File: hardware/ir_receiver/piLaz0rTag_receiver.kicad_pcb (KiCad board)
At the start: 2 copper layers, 5 parts

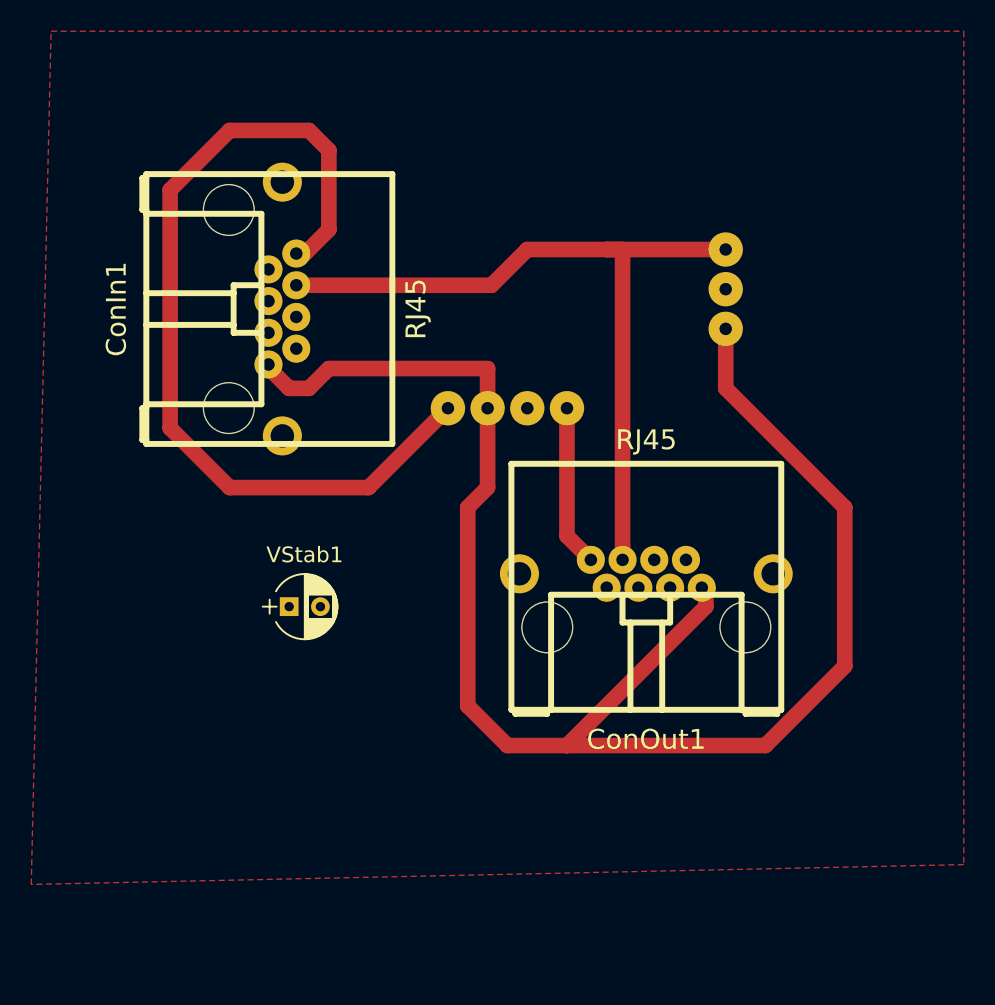
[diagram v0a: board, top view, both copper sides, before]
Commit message: Add Dome as drawing
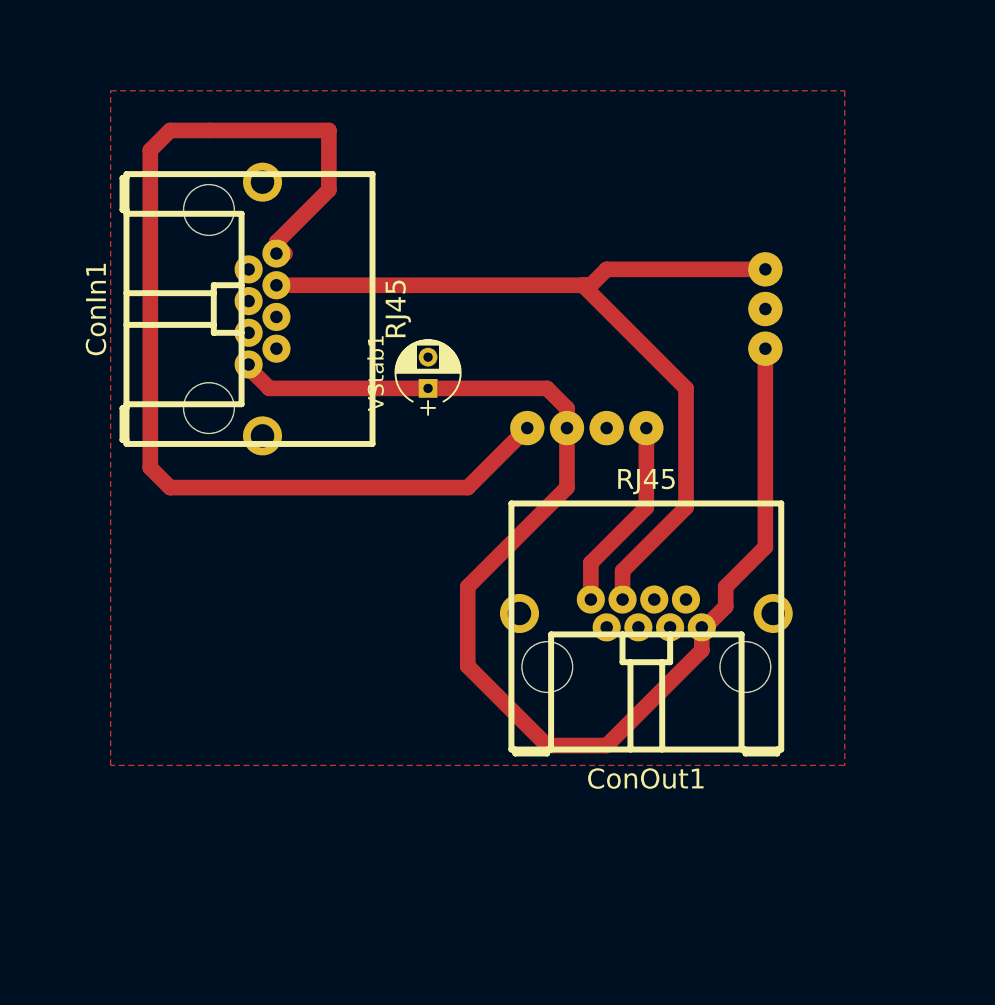
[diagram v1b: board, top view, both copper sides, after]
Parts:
- moved VStab1 16.6 mm to (97.8, 102.9), turned to 90 degrees
- moved LED1 5.24 mm to (111.8, 105.4)
- moved IR_REC1 2.84 mm to (119.4, 95.2)
- moved ConOut1 2.54 mm to (111.8, 118.1)
- moved ConIn1 1.27 mm to (86.4, 97.8)
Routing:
- net +5V: track 103.8 -> 81.9 mm
- net /LedIn: track 57.1 -> 68.7 mm
- net /IrData: track 49.7 -> 57.1 mm
- net /LedOut: track 10.7 -> 12.8 mm

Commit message: First thing to test
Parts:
- added REF**: MountingHole_2.2mm_M2_DIN965, Mounting_Holes:MountingHole_2.2mm_M2_DIN965, F.Cu at (104.1, 99.7)
- added REF**: MountingHole_2.2mm_M2, Mounting_Holes:MountingHole_2.2mm_M2, F.Cu at (115.6, 98.4)
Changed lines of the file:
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@@
 (kicad_pcb (version 4) (host pcbnew 4.0.7-e2-6376~61~ubuntu18.04.1)
   (general
-    (links 18)
-    (no_connects 4)
-    (area 72.39 80.01 132.080001 134.620001)
+    (links 20)
+    (no_connects 5)
+    (area 74.8618 83.82 125.427143 142.400001)
     (thickness 1.6)
     (drawings 8)
     (tracks 45)
     (zones 0)
-    (modules 5)
+    (modules 7)
     (nets 12)
   )
@@
     (mod_text_width 0.15)
     (pad_size 2.2 2.2)
-    (pad_drill 0.8)
+    (pad_drill 0.9)
     (pad_to_mask_clearance 0.2)
     (aux_axis_origin 77.47 127)
@@
     )
   )
+  (module Mounting_Holes:MountingHole_2.2mm_M2_DIN965 (layer F.Cu)
+    (at 104.14 99.695)
+    (descr "Mounting Hole 2.2mm, no annular, M2, DIN965")
+    (tags "mounting hole 2.2mm no annular m2 din965")
+    (fp_text reference REF** (at 0 -2.9) (layer F.SilkS)
+      (effects (font (size 1 1) (thickness 0.15)))
+    )
+    (fp_text value MountingHole_2.2mm_M2_DIN965 (at 0 2.9) (layer F.Fab)
+      (effects (font (size 1 1) (thickness 0.15)))
+    )
+    (fp_circle (center 0 0) (end 1.9 0) (layer Cmts.User) (width 0.15))
+    (fp_circle (center 0 0) (end 2.15 0) (layer F.CrtYd) (width 0.05))
+    (pad 1 thru_hole circle (at 0 0) (size 2.2 2.2) (drill 0.9) (layers *.Cu *.Mask)
+      (net 2 GND))
+  )
+  (module Mounting_Holes:MountingHole_2.2mm_M2 (layer F.Cu)
+    (at 115.57 98.425)
+    (descr "Mounting Hole 2.2mm, no annular, M2")
+    (tags "mounting hole 2.2mm no annular m2")
+    (fp_text reference REF** (at 0 -3.2) (layer F.SilkS)
+      (effects (font (size 1 1) (thickness 0.15)))
+    )
+    (fp_text value MountingHole_2.2mm_M2 (at 0 3.2) (layer F.Fab)
+      (effects (font (size 1 1) (thickness 0.15)))
+    )
+    (fp_circle (center 0 0) (end 2.2 0) (layer Cmts.User) (width 0.15))
+    (fp_circle (center 0 0) (end 2.45 0) (layer F.CrtYd) (width 0.05))
+    (pad 1 thru_hole circle (at 0 0) (size 2.2 2.2) (drill 0.9) (layers *.Cu *.Mask)
+      (net 2 GND))
+  )
   (dimension 21.59 (width 0.3) (layer Dwgs.User)
     (gr_text "21,590 mm" (at 89.535 135.97) (layer Dwgs.User)
@@
   (gr_line (start 101.6 97.79) (end 101.6 87.63) (angle 90) (layer Dwgs.User) (width 0.2))
   (gr_circle (center 111.76 97.73) (end 111.76 87.73) (layer Dwgs.User) (width 0.2))
-  (segment (start 115.31092 118.16588) (end 115.51412 118.16588) (width 1) (layer F.Cu) (net 1) (status C00000))
-  (segment (start 115.51412 118.16588) (end 116.84 116.84) (width 1) (layer F.Cu) (net 1) (status 400000))
-  (segment (start 119.38 113.03) (end 119.38 100.33) (width 1) (layer F.Cu) (net 1) (status 800000))
+  (segment (start 115.31092 118.16588) (end 115.51412 118.16588) (width 1) (layer F.Cu) (net 1))
+  (segment (start 115.51412 118.16588) (end 116.84 116.84) (width 1) (layer F.Cu) (net 1))
+  (segment (start 119.38 113.03) (end 119.38 100.33) (width 1) (layer F.Cu) (net 1))
   (segment (start 116.84 115.57) (end 119.38 113.03) (width 1) (layer F.Cu) (net 1))
   (segment (start 116.84 116.84) (end 116.84 115.57) (width 1) (layer F.Cu) (net 1))

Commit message: First thing to test
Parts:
- ConIn1, ConOut1, REF** (x2), VStab1: moved to B.Cu
- IR_REC1, LED1: moved to F.Cu
- moved IR_REC1 33.7 mm to (119.4, 128.9), turned to 90 degrees
- moved ConIn1 28.6 mm to (86.4, 126.4), turned to 90 degrees
- moved REF** 27.3 mm to (115.6, 125.7)
- moved REF** 24.8 mm to (104.1, 124.5)
- moved VStab1 18.4 mm to (97.8, 121.3), turned to 270 degrees
- moved LED1 13.3 mm to (111.8, 118.7), turned to 270 degrees
- moved ConOut1 12.1 mm to (111.8, 106.0)
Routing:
- added copper zone on B.Cu, net GND
- removed copper zone on F.Cu, net GND

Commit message: First thing to test
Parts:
- removed REF**: MountingHole_2.2mm_M2_DIN965, Mounting_Holes:MountingHole_2.2mm_M2_DIN965
- removed REF**: MountingHole_2.2mm_M2, Mounting_Holes:MountingHole_2.2mm_M2
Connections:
- ConIn1 pad 13: Net-(ConIn1-Pad13) -> GND
- ConIn1 pad 2: Net-(ConIn1-Pad2) -> GND
- ConIn1 pad 3: Net-(ConIn1-Pad3) -> GND
- ConOut1 pad 13: Net-(ConOut1-Pad13) -> GND
- ConOut1 pad 2: Net-(ConOut1-Pad2) -> GND
- ConOut1 pad 3: Net-(ConOut1-Pad3) -> GND
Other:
- net class Default: via_dia 0.6 -> 1; via_drill 0.4 -> 0.9
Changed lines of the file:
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@@
 (kicad_pcb (version 4) (host pcbnew 4.0.7-e2-6376~61~ubuntu18.04.1)
   (general
-    (links 20)
-    (no_connects 4)
-    (area 74.8618 83.82 125.427143 142.400001)
+    (links 24)
+    (no_connects 1)
+    (area 74.8618 94.5468 124.690001 140.335001)
     (thickness 1.6)
     (drawings 6)
-    (tracks 45)
+    (tracks 44)
     (zones 0)
-    (modules 7)
-    (nets 12)
+    (modules 5)
+    (nets 6)
   )
   (page A4)
@@
     (segment_width 0.2)
     (edge_width 0.15)
-    (via_size 0.6)
-    (via_drill 0.4)
+    (via_size 1)
+    (via_drill 0.9)
     (via_min_size 0.4)
     (via_min_drill 0.3)
@@
     (mod_text_size 1 1)
     (mod_text_width 0.15)
-    (pad_size 2.2 2.2)
-    (pad_drill 0.9)
+    (pad_size 0.8 0.8)
+    (pad_drill 0.8)
     (pad_to_mask_clearance 0.2)
     (aux_axis_origin 77.47 127)
@@
   (net 4 /LedIn)
   (net 5 /LedOut)
-  (net 6 "Net-(ConIn1-Pad2)")
-  (net 7 "Net-(ConIn1-Pad13)")
-  (net 8 "Net-(ConOut1-Pad2)")
-  (net 9 "Net-(ConOut1-Pad13)")
-  (net 10 "Net-(ConIn1-Pad3)")
-  (net 11 "Net-(ConOut1-Pad3)")
   (net_class Default "This is the default net class."
     (clearance 0.5)
     (trace_width 1)
-    (via_dia 0.6)
-    (via_drill 0.4)
+    (via_dia 1)
+    (via_drill 0.9)
     (uvia_dia 0.3)
     (uvia_drill 0.1)
@@
     (add_net /LedOut)
     (add_net GND)
-    (add_net "Net-(ConIn1-Pad13)")
-    (add_net "Net-(ConIn1-Pad2)")
-    (add_net "Net-(ConIn1-Pad3)")
-    (add_net "Net-(ConOut1-Pad13)")
-    (add_net "Net-(ConOut1-Pad2)")
-    (add_net "Net-(ConOut1-Pad3)")
   )
   (module kicad:rj45-seppel-small (layer B.Cu)
@@
     (fp_line (start 8.636 7.874) (end 8.636 -7.874) (layer B.SilkS) (width 0.381))
     (fp_line (start 8.636 -7.874) (end -8.636 -7.874) (layer B.SilkS) (width 0.381))
-    (pad 3 thru_hole circle (at 1.52146 -0.05588) (size 1.8 1.8) (drill 0.8001) (layers *.Cu *.Mask)
-      (net 11 "Net-(ConOut1-Pad3)"))
-    (pad 1 thru_hole circle (at 3.55092 -0.05588) (size 1.8 1.8) (drill 0.8001) (layers *.Cu *.Mask)
+    (pad 3 thru_hole circle (at 1.52146 -0.05588) (size 0.8 0.8) (drill 0.8) (layers *.Cu *.Mask)
+      (net 2 GND))
+    (pad 1 thru_hole circle (at 3.55092 -0.05588) (size 2.2 2.2) (drill 0.8) (layers *.Cu *.Mask)
       (net 1 +5V))
-    (pad 2 thru_hole circle (at 2.53746 1.72466) (size 1.8 1.8) (drill 0.8001) (layers *.Cu *.Mask)
-      (net 8 "Net-(ConOut1-Pad2)"))
-    (pad 4 thru_hole circle (at 0.508 1.72466) (size 1.8 1.8) (drill 0.8001) (layers *.Cu *.Mask)
-      (net 2 GND))
-    (pad 5 thru_hole circle (at -0.508 -0.05588) (size 1.8 1.8) (drill 0.8001) (layers *.Cu *.Mask)
+    (pad 2 thru_hole circle (at 2.53746 1.72466) (size 0.8 0.8) (drill 0.8) (layers *.Cu *.Mask)
+      (net 2 GND))
+    (pad 4 thru_hole circle (at 0.508 1.72466) (size 0.8 0.8) (drill 0.8) (layers *.Cu *.Mask)
+      (net 2 GND))
+    (pad 5 thru_hole circle (at -0.508 -0.05588) (size 0.8 0.8) (drill 0.8) (layers *.Cu *.Mask)
       (net 2 GND))
     (pad 6 thru_hole circle (at -1.52146 1.72466) (size 1.8 1.8) (drill 0.8001) (layers *.Cu *.Mask)
       (net 3 /IrData))
-    (pad 7 thru_hole circle (at -2.53746 -0.05588) (size 1.8 1.8) (drill 0.8001) (layers *.Cu *.Mask)
+    (pad 7 thru_hole circle (at -2.53746 -0.05588) (size 0.8 0.8) (drill 0.8) (layers *.Cu *.Mask)
       (net 2 GND))
     (pad 8 thru_hole circle (at -3.55092 1.72466) (size 1.8 1.8) (drill 0.8) (layers *.Cu *.Mask)
       (net 5 /LedOut))
-    (pad 13 thru_hole circle (at -8.12038 0.83312) (size 2.49936 2.49936) (drill 1.50114) (layers *.Cu *.Mask)
-      (net 9 "Net-(ConOut1-Pad13)"))
-    (pad 13 thru_hole circle (at 8.12038 0.83312) (size 2.49936 2.49936) (drill 1.50114) (layers *.Cu *.Mask)
-      (net 9 "Net-(ConOut1-Pad13)"))
+    (pad 13 thru_hole circle (at -8.12038 0.83312) (size 2.49936 2.49936) (drill 2.49936) (layers *.Cu *.Mask)
+      (net 2 GND))
+    (pad 13 thru_hole circle (at 8.12038 0.83312) (size 2.49936 2.49936) (drill 2.49936) (layers *.Cu *.Mask)
+      (net 2 GND))
     (pad "" np_thru_hole circle (at -6.33984 -2.59588) (size 3.2512 3.2512) (drill 3.2512) (layers *.Cu))
     (pad "" np_thru_hole circle (at 6.33984 -2.59588) (size 3.2512 3.2512) (drill 3.2512) (layers *.Cu))
@@
     (fp_line (start 8.636 7.874) (end 8.636 -7.874) (layer B.SilkS) (width 0.381))
     (fp_line (start 8.636 -7.874) (end -8.636 -7.874) (layer B.SilkS) (width 0.381))
-    (pad 3 thru_hole circle (at 1.52146 -0.05588 90) (size 1.8 1.8) (drill 0.8001) (layers *.Cu *.Mask)
-      (net 10 "Net-(ConIn1-Pad3)"))
-    (pad 1 thru_hole circle (at 3.55092 -0.05588 90) (size 1.8 1.8) (drill 0.8001) (layers *.Cu *.Mask)
+    (pad 3 thru_hole circle (at 1.52146 -0.05588 90) (size 0.8 0.8) (drill 0.8) (layers *.Cu *.Mask)
+      (net 2 GND))
+    (pad 1 thru_hole circle (at 3.55092 -0.05588 90) (size 2.2 2.2) (drill 0.9) (layers *.Cu *.Mask)
       (net 1 +5V))
-    (pad 2 thru_hole circle (at 2.53746 1.72466 90) (size 1.8 1.8) (drill 0.8001) (layers *.Cu *.Mask)
-      (net 6 "Net-(ConIn1-Pad2)"))
-    (pad 4 thru_hole circle (at 0.508 1.72466 90) (size 1.8 1.8) (drill 0.8001) (layers *.Cu *.Mask)
-      (net 2 GND))
-    (pad 5 thru_hole circle (at -0.508 -0.05588 90) (size 1.8 1.8) (drill 0.8001) (layers *.Cu *.Mask)
-      (net 2 GND))
-    (pad 6 thru_hole circle (at -1.52146 1.72466 90) (size 1.8 1.8) (drill 0.8001) (layers *.Cu *.Mask)
+    (pad 2 thru_hole circle (at 2.53746 1.72466 90) (size 0.8 0.8) (drill 0.8) (layers *.Cu *.Mask)
+      (net 2 GND))
+    (pad 4 thru_hole circle (at 0.508 1.72466 90) (size 0.8 0.8) (drill 0.8) (layers *.Cu *.Mask)
+      (net 2 GND))
+    (pad 5 thru_hole circle (at -0.508 -0.05588 90) (size 0.8 0.8) (drill 0.8) (layers *.Cu *.Mask)
+      (net 2 GND))
+    (pad 6 thru_hole circle (at -1.52146 1.72466 90) (size 1.9 1.9) (drill 0.9) (layers *.Cu *.Mask)
       (net 3 /IrData))
-    (pad 7 thru_hole circle (at -2.53746 -0.05588 90) (size 1.8 1.8) (drill 0.8001) (layers *.Cu *.Mask)
-      (net 2 GND))
-    (pad 8 thru_hole circle (at -3.55092 1.72466 90) (size 1.8 1.8) (drill 0.8) (layers *.Cu *.Mask)
+    (pad 7 thru_hole circle (at -2.53746 -0.05588 90) (size 0.8 0.8) (drill 0.8) (layers *.Cu *.Mask)
+      (net 2 GND))
+    (pad 8 thru_hole circle (at -3.55092 1.72466 90) (size 1.9 1.9) (drill 0.9) (layers *.Cu *.Mask)
       (net 4 /LedIn))
-    (pad 13 thru_hole circle (at -8.12038 0.83312 90) (size 2.49936 2.49936) (drill 1.50114) (layers *.Cu *.Mask)
-      (net 7 "Net-(ConIn1-Pad13)"))
-    (pad 13 thru_hole circle (at 8.12038 0.83312 90) (size 2.49936 2.49936) (drill 1.50114) (layers *.Cu *.Mask)
-      (net 7 "Net-(ConIn1-Pad13)"))
+    (pad 13 thru_hole circle (at -8.12038 0.83312 90) (size 2.49936 2.49936) (drill 2.49936) (layers *.Cu *.Mask)
+      (net 2 GND))
+    (pad 13 thru_hole circle (at 8.12038 0.83312 90) (size 2.49936 2.49936) (drill 2.49936) (layers *.Cu *.Mask)
+      (net 2 GND))
     (pad "" np_thru_hole circle (at -6.33984 -2.59588 90) (size 3.2512 3.2512) (drill 3.2512) (layers *.Cu))
     (pad "" np_thru_hole circle (at 6.33984 -2.59588 90) (size 3.2512 3.2512) (drill 3.2512) (layers *.Cu))
@@
     )
   )
-  (module Mounting_Holes:MountingHole_2.2mm_M2_DIN965 (layer B.Cu)
-    (at 104.14 124.46)
-    (descr "Mounting Hole 2.2mm, no annular, M2, DIN965")
-    (tags "mounting hole 2.2mm no annular m2 din965")
-    (fp_text reference REF** (at 0 2.9) (layer B.SilkS)
-      (effects (font (size 1 1) (thickness 0.15)) (justify mirror))
-    )
-    (fp_text value MountingHole_2.2mm_M2_DIN965 (at 0 -2.9) (layer B.Fab)
-      (effects (font (size 1 1) (thickness 0.15)) (justify mirror))
-    )
-    (fp_circle (center 0 0) (end 1.9 0) (layer Cmts.User) (width 0.15))
-    (fp_circle (center 0 0) (end 2.15 0) (layer B.CrtYd) (width 0.05))
-    (pad 1 thru_hole circle (at 0 0) (size 2.2 2.2) (drill 0.9) (layers *.Cu *.Mask)
-      (net 2 GND))
-  )
-  (module Mounting_Holes:MountingHole_2.2mm_M2 (layer B.Cu)
-    (at 115.57 125.73)
-    (descr "Mounting Hole 2.2mm, no annular, M2")
-    (tags "mounting hole 2.2mm no annular m2")
-    (fp_text reference REF** (at 0 3.2) (layer B.SilkS)
-      (effects (font (size 1 1) (thickness 0.15)) (justify mirror))
-    )
-    (fp_text value MountingHole_2.2mm_M2 (at 0 -3.2) (layer B.Fab)
-      (effects (font (size 1 1) (thickness 0.15)) (justify mirror))
-    )
-    (fp_circle (center 0 0) (end 2.2 0) (layer Cmts.User) (width 0.15))
-    (fp_circle (center 0 0) (end 2.45 0) (layer B.CrtYd) (width 0.05))
-    (pad 1 thru_hole circle (at 0 0) (size 2.2 2.2) (drill 0.9) (layers *.Cu *.Mask)
-      (net 2 GND))
-  )
   (gr_line (start 101.6 116.205) (end 101.6 126.365) (angle 90) (layer Dwgs.User) (width 0.2))
   (gr_line (start 121.92 116.205) (end 101.6 116.205) (angle 90) (layer Dwgs.User) (width 0.2))
@@
   (segment (start 108.20908 110.11408) (end 111.76 113.665) (width 1) (layer B.Cu) (net 5))
   (segment (start 107.95 108.02874) (end 108.20908 107.76966) (width 1) (layer B.Cu) (net 5) (status 30))
-  (segment (start 114.3 107.7722) (end 114.29746 107.76966) (width 1) (layer B.Cu) (net 8) (status 30))
   (zone (net 2) (net_name GND) (layer B.Cu) (hatch edge 0.508)
     (connect_pads yes (clearance 0.6))
